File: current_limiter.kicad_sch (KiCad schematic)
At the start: 62 parts, among them J1 73096-2, J2 73096-2, J3 CS-, J4 CS+, J5 73096-2, J6 73096-2, Q1 ISC025N08NM5LF2, Q2 BC849, Q3 BC858, U1 TLV1805QDBVRQ1, U2 ZXCT181A2W6-7, U3 OPA991IDCKR, U4 BAT54CLT3G, U5 LM4040DIM3-2.5/NOPB, U6 AP63203QWU-7

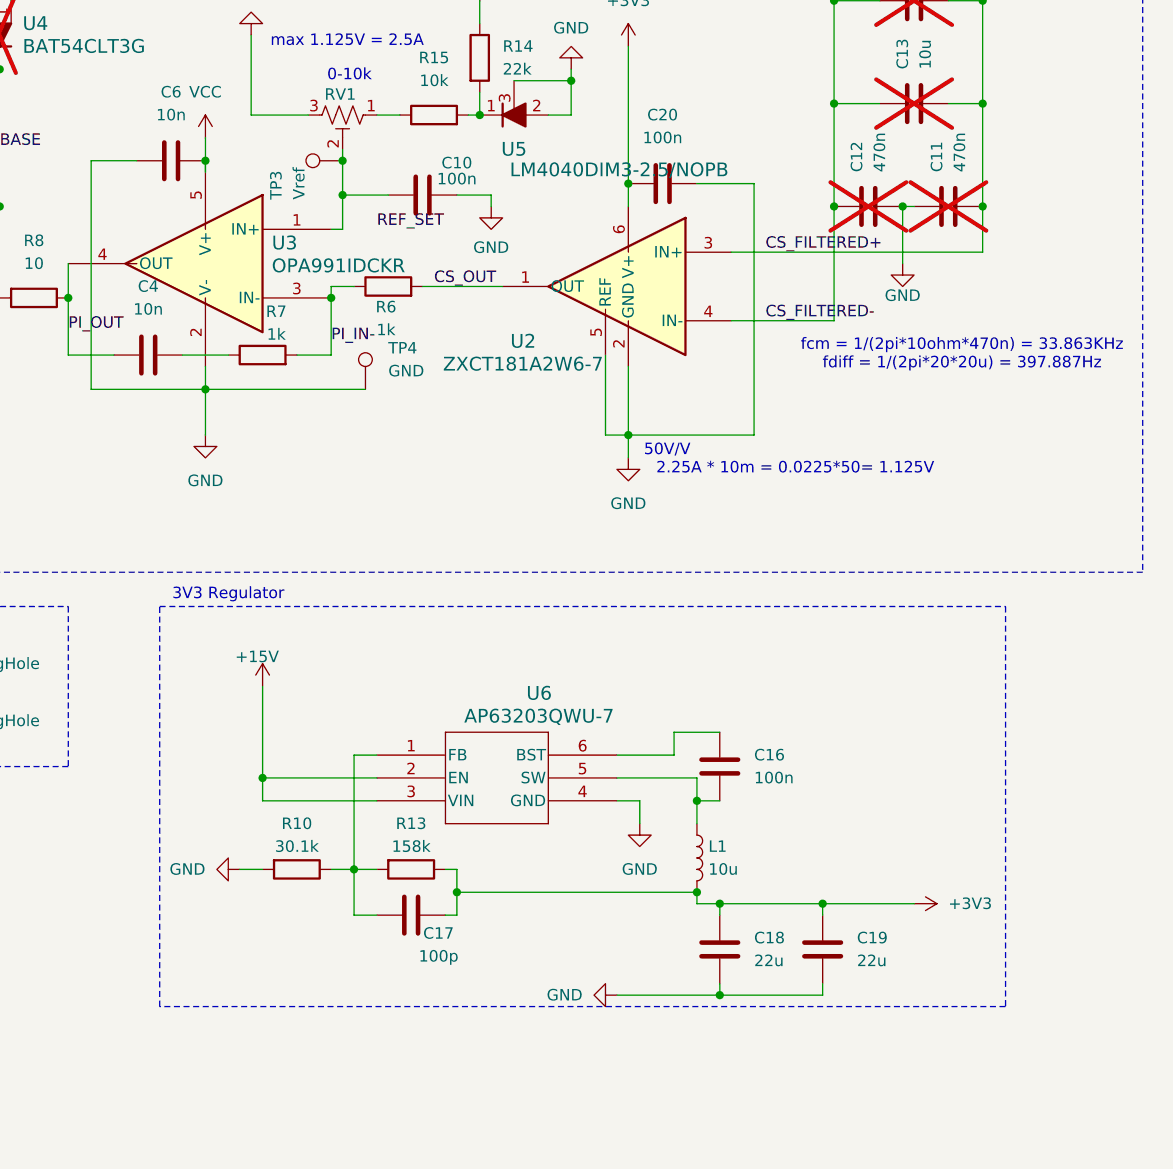
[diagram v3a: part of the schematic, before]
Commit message: updated 3v3 reg to be correct ala datasheet
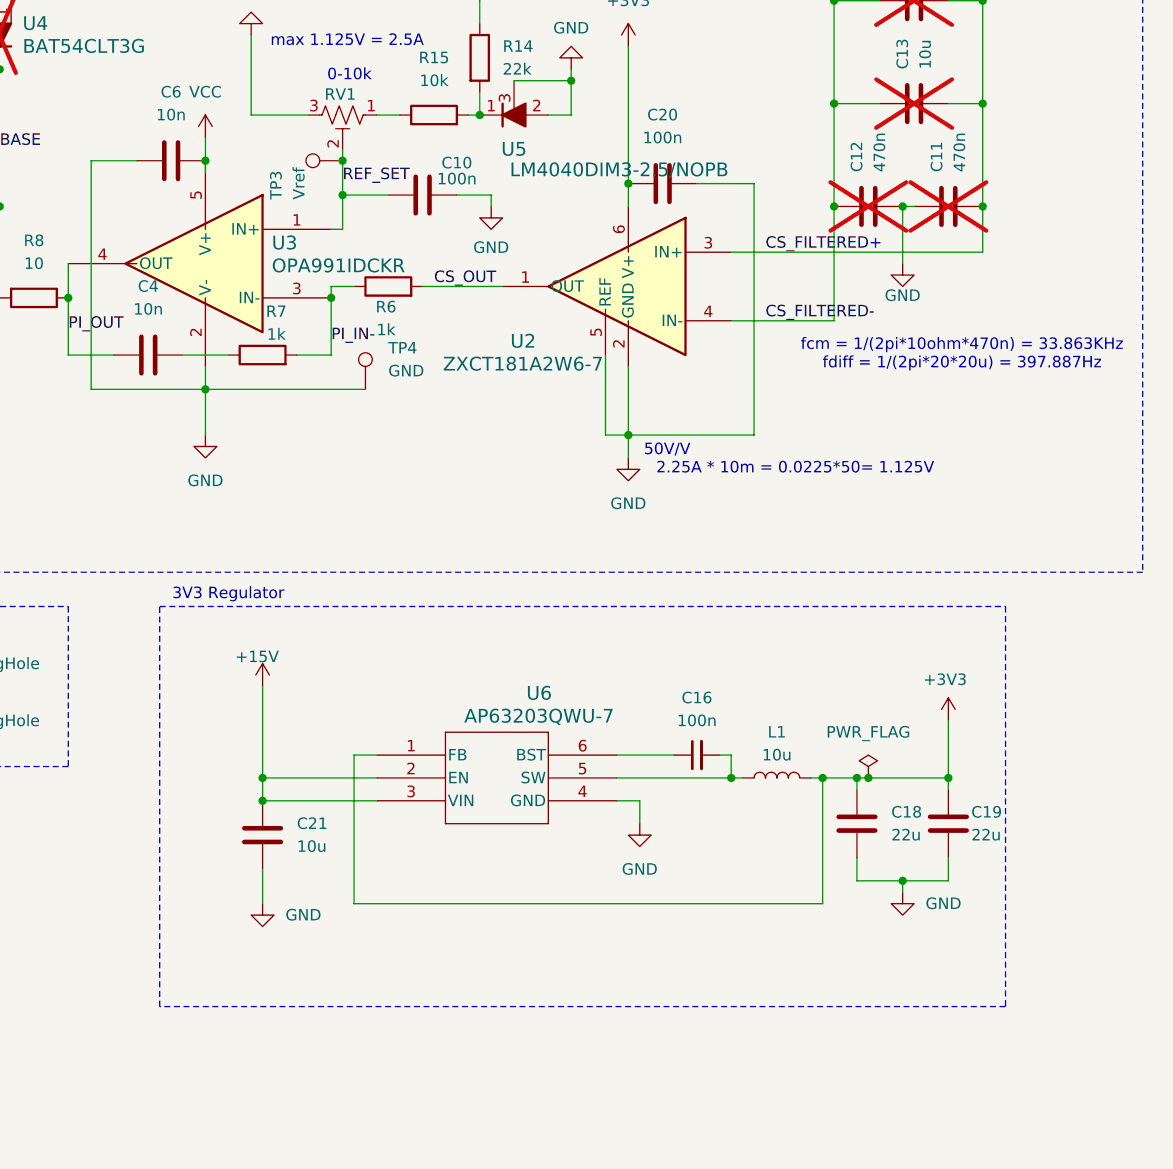
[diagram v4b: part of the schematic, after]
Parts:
- removed C16: 100n, Capacitor_SMD:C_0805_2012Metric, symbol Device:C
- removed C17: 100p, Capacitor_SMD:C_0805_2012Metric, symbol Device:C
- removed R10: 30.1k, Resistor_SMD:R_0805_2012Metric, symbol Device:R
- removed R13: 158k, Resistor_SMD:R_0805_2012Metric, symbol Device:R
- added C16: 100n, Capacitor_SMD:C_0805_2012Metric, symbol Device:C_Small
- added C21: 10u, Capacitor_SMD:C_0805_2012Metric, symbol Device:C
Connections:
- net +15V: now also C21.1
- net +3V3: now also U6.1 (FB)
- net GND: now also C21.2
- net REF_SET: now also C10.2, RV1.2, TP3.1, U3.1 (IN+)
- net at L1.1, U6.5 (SW): now also C16.2
- net at U6.6 (BST): now also C16.1
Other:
- moved on the sheet: C18, C19, L1

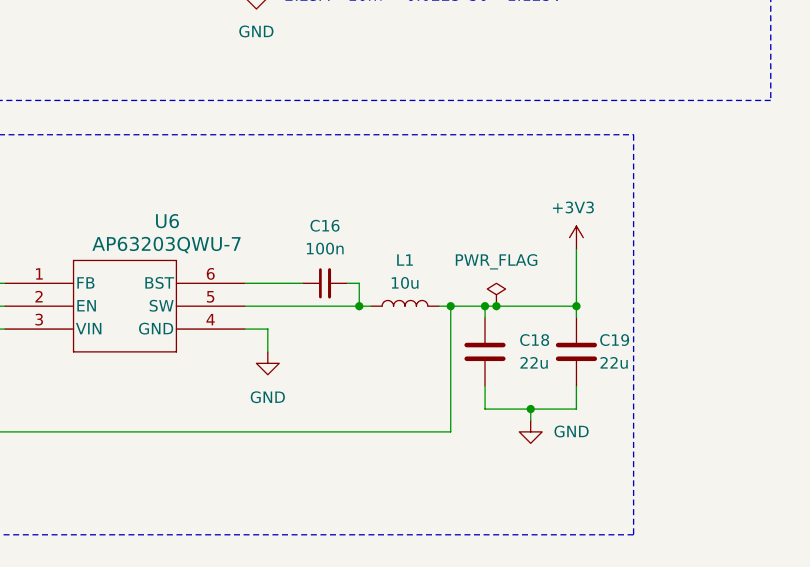
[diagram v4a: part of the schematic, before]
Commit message: minor changes including changing to more viable inductor footprint & correct inductor sizing
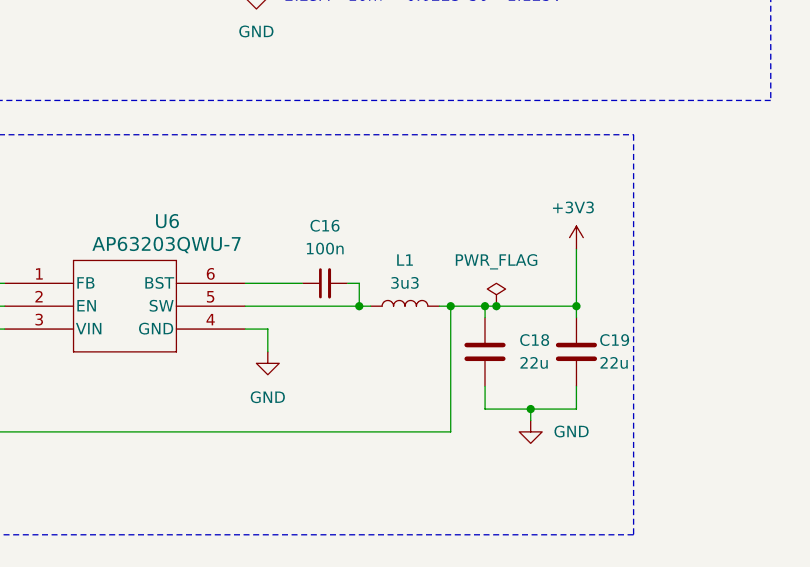
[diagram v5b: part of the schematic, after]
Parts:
- L1: value 10u -> 3u3; footprint Inductor_SMD:L_0805_2012Metric -> Current_Limiter_Stuff:IND_BOURNS_SDR0302
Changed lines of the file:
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@@
 			)
 		)
-		(property "Value" "10u"
+		(property "Value" "3u3"
 			(at 241.3 137.16 90)
 			(show_name no)
@@
 			)
 		)
-		(property "Footprint" "Inductor_SMD:L_0805_2012Metric"
+		(property "Footprint" "Current_Limiter_Stuff:IND_BOURNS_SDR0302"
 			(at 241.3 139.7 0)
 			(hide yes)
